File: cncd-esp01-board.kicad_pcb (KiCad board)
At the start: 2 copper layers, 29 x 39 mm, 30 parts, among them J1 ESP, J2 CTRL, SW1 RESET, T1 Fiducial_1mm_Mask2mm, T2 Fiducial_1mm_Mask2mm, U1 TL431DBZ, U2 AMS1117-3.3, U3 SN74AHC1G04DBVR, U4 SN74LVC1G126DBVR, U5 SN74LVC1G126DBVR, U6 SN74LVC1T45DBVR

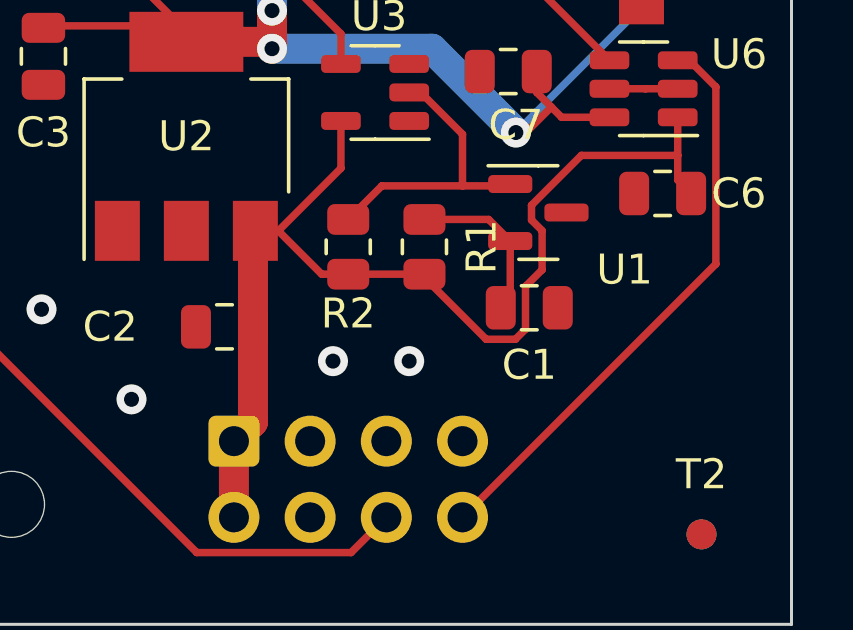
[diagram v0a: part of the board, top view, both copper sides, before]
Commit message: Add 100uF bypass capacitor to mitigate #1
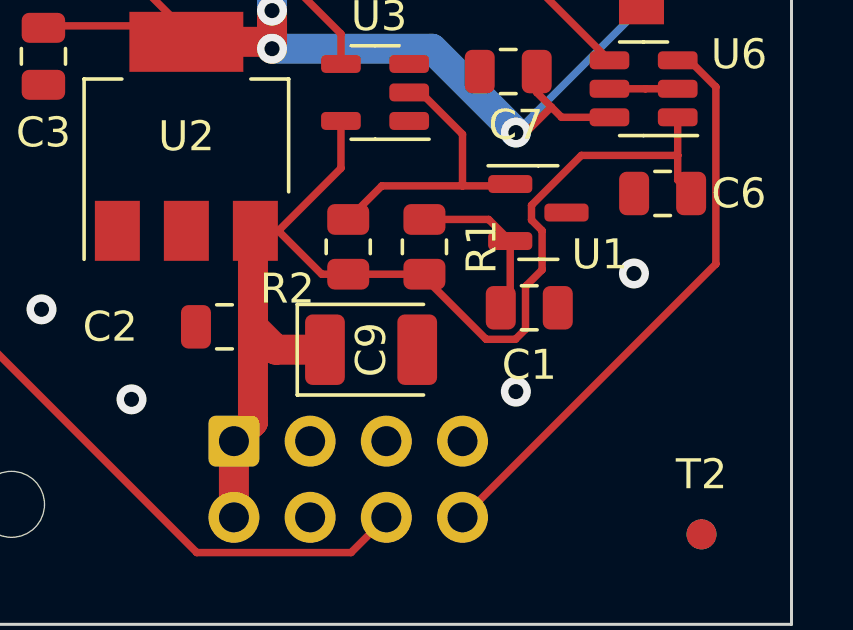
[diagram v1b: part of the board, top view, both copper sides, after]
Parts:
- added C9: 100uF, Capacitor_Tantalum_SMD:CP_EIA-3528-21_Kemet-B, F.Cu at (15.0, 29.8)
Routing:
- net +5V: track 37.9 -> 40.6 mm
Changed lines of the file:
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@@
     (property "ki_keywords" "diode device shunt regulator")
     (attr smd)
-    (fp_text reference "U1" (at 2.8725 1.905) (layer "F.SilkS")
+    (fp_text reference "U1" (at 2.0445 1.397) (layer "F.SilkS")
         (effects (font (size 1 1) (thickness 0.15)))
     )
@@
     (pad "" np_thru_hole circle (at 0 0) (size 2.2 2.2) (drill 2.2) (layers "*.Cu" "*.Mask"))
   )
+  (footprint "Capacitor_Tantalum_SMD:CP_EIA-3528-21_Kemet-B" (layer "F.Cu")
+    (at 14.986 29.845)
+    (descr "Tantalum Capacitor SMD Kemet-B (3528-21 Metric), IPC_7351 nominal, (Body size from: http://www.kemet.com/Lists/ProductCatalog/Attachments/253/KEM_TC101_STD.pdf), generated with kicad-footprint-generator")
+    (tags "capacitor tantalum")
+    (property "Sheetfile" "cncd-esp01-board.kicad_sch")
+    (property "Sheetname" "")
+    (property "ki_description" "Polarized capacitor")
+    (property "ki_keywords" "cap capacitor")
+    (attr smd)
+    (fp_text reference "C9" (at 0 0 90) (layer "F.SilkS")
+        (effects (font (size 1 1) (thickness 0.15)))
+    )
+    (fp_text value "100uF" (at 0 2.35) (layer "F.Fab")
+        (effects (font (size 1 1) (thickness 0.15)))
+    )
+    (fp_text user "${REFERENCE}" (at 0 0) (layer "F.Fab")
+        (effects (font (size 0.88 0.88) (thickness 0.13)))
+    )
+    (fp_line (start -2.46 -1.51) (end -2.46 1.51)
+      (stroke (width 0.12) (type solid)) (layer "F.SilkS"))
+    (fp_line (start -2.46 1.51) (end 1.75 1.51)
+      (stroke (width 0.12) (type solid)) (layer "F.SilkS"))
+    (fp_line (start 1.75 -1.51) (end -2.46 -1.51)
+      (stroke (width 0.12) (type solid)) (layer "F.SilkS"))
+    (fp_line (start -2.45 -1.65) (end 2.45 -1.65)
+      (stroke (width 0.05) (type solid)) (layer "F.CrtYd"))
+    (fp_line (start -2.45 1.65) (end -2.45 -1.65)
+      (stroke (width 0.05) (type solid)) (layer "F.CrtYd"))
+    (fp_line (start 2.45 -1.65) (end 2.45 1.65)
+      (stroke (width 0.05) (type solid)) (layer "F.CrtYd"))
+    (fp_line (start 2.45 1.65) (end -2.45 1.65)
+      (stroke (width 0.05) (type solid)) (layer "F.CrtYd"))
+    (fp_line (start -1.75 -0.7) (end -1.75 1.4)
+      (stroke (width 0.1) (type solid)) (layer "F.Fab"))
+    (fp_line (start -1.75 1.4) (end 1.75 1.4)
+      (stroke (width 0.1) (type solid)) (layer "F.Fab"))
+    (fp_line (start -1.05 -1.4) (end -1.75 -0.7)
+      (stroke (width 0.1) (type solid)) (layer "F.Fab"))
+    (fp_line (start 1.75 -1.4) (end -1.05 -1.4)
+      (stroke (width 0.1) (type solid)) (layer "F.Fab"))
+    (fp_line (start 1.75 1.4) (end 1.75 -1.4)
+      (stroke (width 0.1) (type solid)) (layer "F.Fab"))
+    (pad "1" smd roundrect (at -1.5375 0) (size 1.325 2.35) (layers "F.Cu" "F.Paste" "F.Mask") (roundrect_rratio 0.188679)
+      (net 3 "+5V") (pintype "passive"))
+    (pad "2" smd roundrect (at 1.5375 0) (size 1.325 2.35) (layers "F.Cu" "F.Paste" "F.Mask") (roundrect_rratio 0.188679)
+      (net 2 "GND") (pintype "passive"))
+    (model "${KICAD6_3DMODEL_DIR}/Capacitor_Tantalum_SMD.3dshapes/CP_EIA-3528-21_Kemet-B.wrl"
+      (offset (xyz 0 0 0))
+      (scale (xyz 1 1 1))
+      (rotate (xyz 0 0 0))
+    )
+  )
   (footprint "Capacitor_SMD:C_0805_2012Metric" (layer "F.Cu")
     (at 10.099 29.083 180)
@@
     (property "ki_keywords" "R resistor")
     (attr smd)
-    (fp_text reference "R2" (at -2.225 0) (layer "F.SilkS")
+    (fp_text reference "R2" (at -1.397 -2.032) (layer "F.SilkS")
         (effects (font (size 1 1) (thickness 0.15)))
     )
@@
   (segment (start 24.13 21.148) (end 25.2065 21.148) (width 0.25) (layer "F.Cu") (net 2))
   (segment (start 22.9315 21.148) (end 24.13 21.148) (width 0.25) (layer "F.Cu") (net 2))
-  (via (at 13.716 30.226) (size 1) (drill 0.5) (layers "F.Cu" "B.Cu") (free) (net 2))
-  (via (at 16.256 30.226) (size 1) (drill 0.5) (layers "F.Cu" "B.Cu") (free) (net 2))
+  (via (at 19.812 31.242) (size 1) (drill 0.5) (layers "F.Cu" "B.Cu") (free) (net 2))
+  (via (at 23.749 27.305) (size 1) (drill 0.5) (layers "F.Cu" "B.Cu") (free) (net 2))
   (via (at 14 17) (size 1) (drill 0.5) (layers "F.Cu" "B.Cu") (free) (net 2))
   (via (at 4 28.5) (size 1) (drill 0.5) (layers "F.Cu" "B.Cu") (free) (net 2))
@@
   (via (at 7 31.5) (size 1) (drill 0.5) (layers "F.Cu" "B.Cu") (free) (net 2))
   (segment (start 20.134 27.734827) (end 20.134 29.161173) (width 0.25) (layer "F.Cu") (net 3))
+  (segment (start 13.4485 29.845) (end 11.811 29.845) (width 1) (layer "F.Cu") (net 3))
   (segment (start 14.224 27.3285) (end 13.341 27.3285) (width 0.25) (layer "F.Cu") (net 3))
   (segment (start 10.414 35.433) (end 10.414 32.893) (width 1) (layer "F.Cu") (net 3))
@@
   (segment (start 20.134 29.161173) (end 19.797173 29.498) (width 0.25) (layer "F.Cu") (net 3))
   (segment (start 20.333249 25.0295) (end 21.994749 23.368) (width 0.25) (layer "F.Cu") (net 3))
+  (segment (start 11.811 29.845) (end 11.049 29.083) (width 1) (layer "F.Cu") (net 3))
   (segment (start 13.981 22.22) (end 13.981 23.7975) (width 0.25) (layer "F.Cu") (net 3))
   (segment (start 16.764 27.441173) (end 16.764 27.3285) (width 0.25) (layer "F.Cu") (net 3))
